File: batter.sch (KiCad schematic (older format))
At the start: 6 parts, among them U2 MCP73831-SOT-23-5, U3 NCP4681-SC-70

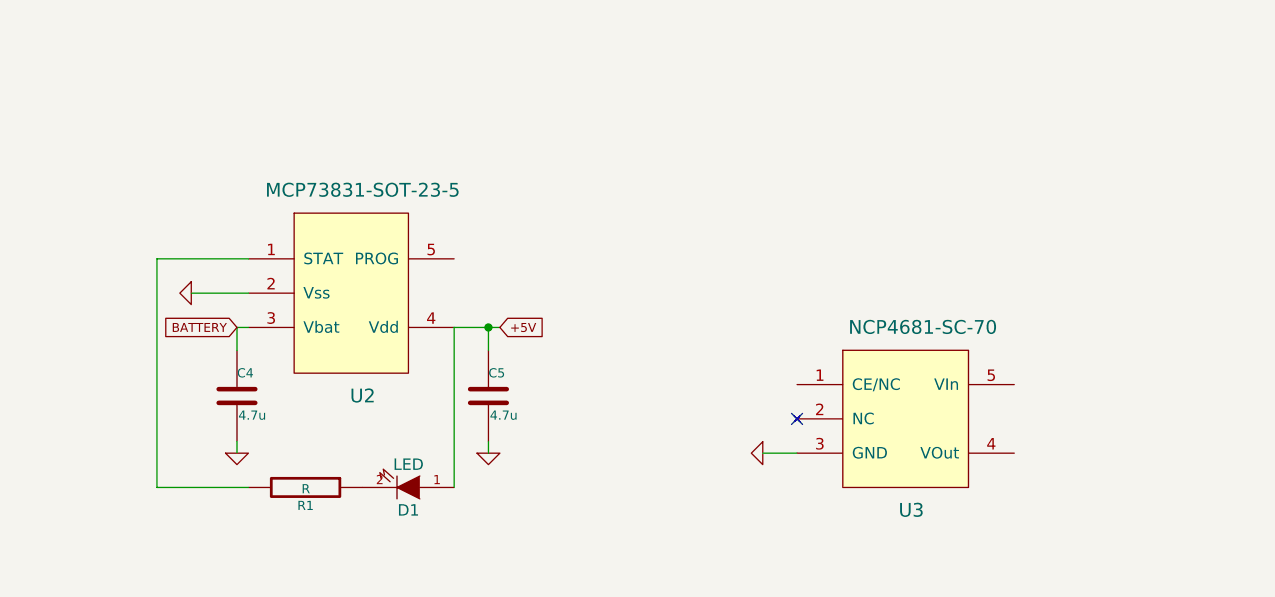
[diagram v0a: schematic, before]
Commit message: Add gps
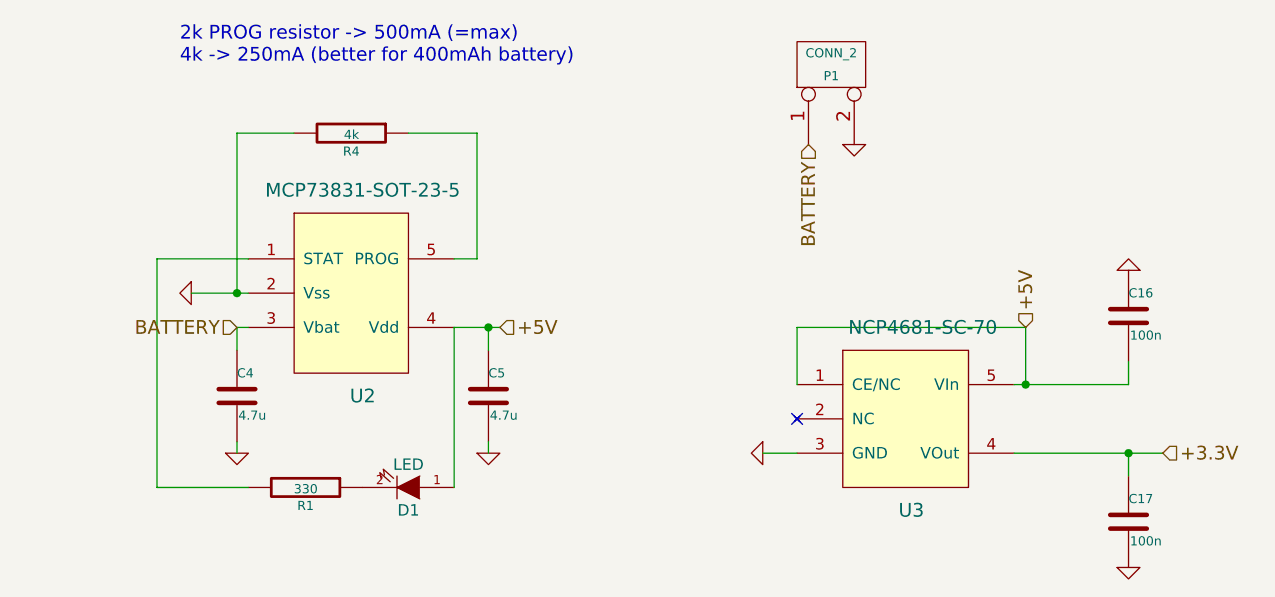
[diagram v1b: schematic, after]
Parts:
- added C16, C17: 100n, symbol C
- added P1: CONN_2, symbol CONN_2
- added R4: 4k, symbol R
- R1: value R -> 330
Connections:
- net +5V: now also U3.1 (CE/NC), U3.5 (VIn), C16.2
- net BATTERY: now also P1.1 (P1)
- net GND: now also C16.1, C17.2, P1.2 (PM), R4.2
- net at U2.5 (PROG): now also R4.1
- net +3.3V: now reaches U3.4 (VOut)
- net +3.3V: now also C17.1
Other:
- note added: "2k PROG resistor -> 500mA (=max)\n4k -> 250mA (better for 400mAh battery)"
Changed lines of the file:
@@
 $Descr A4 11693 8268
 encoding utf-8
-Sheet 3 10
+Sheet 3 11
 Title ""
 Date ""
@@
 $EndComp
 $Comp
-L GND #PWR3
+L GND #PWR4
 U 1 1 54461EBB
 P 3100 2200
-F 0 "#PWR3" H 3100 2200 30  0001 C CNN
+F 0 "#PWR4" H 3100 2200 30  0001 C CNN
 F 1 "GND" H 3100 2130 30  0001 C CNN
 F 2 "" H 3100 2200 60  0000 C CNN
@@
 	0    1    1    0
 $EndComp
-Text GLabel 4450 2350 2    39   Input ~ 0
-+5V
-Text GLabel 3300 2350 0    39   Input ~ 0
-BATTERY
 $Comp
 L LED D1
@@
 P 3600 3050
 F 0 "R1" V 3680 3050 40  0000 C CNN
-F 1 "R" V 3607 3051 40  0000 C CNN
+F 1 "330" V 3607 3051 40  0000 C CNN
 F 2 "" V 3530 3050 30  0001 C CNN
 F 3 "" H 3600 3050 30  0000 C CNN
@@
 $EndComp
 $Comp
-L GND #PWR5
+L GND #PWR6
 U 1 1 54461ED8
 P 4400 2900
-F 0 "#PWR5" H 4400 2900 30  0001 C CNN
+F 0 "#PWR6" H 4400 2900 30  0001 C CNN
 F 1 "GND" H 4400 2830 30  0001 C CNN
 F 2 "" H 4400 2900 60  0000 C CNN
@@
 $EndComp
 $Comp
-L GND #PWR4
+L GND #PWR5
 U 1 1 54461EDE
 P 3300 2900
-F 0 "#PWR4" H 3300 2900 30  0001 C CNN
+F 0 "#PWR5" H 3300 2900 30  0001 C CNN
 F 1 "GND" H 3300 2830 30  0001 C CNN
 F 2 "" H 3300 2900 60  0000 C CNN
@@
 NoConn ~ 5750 2750
 $Comp
-L GND #PWR6
+L GND #PWR7
 U 1 1 5446543B
 P 5600 2900
-F 0 "#PWR6" H 5600 2900 30  0001 C CNN
+F 0 "#PWR7" H 5600 2900 30  0001 C CNN
 F 1 "GND" H 5600 2830 30  0001 C CNN
 F 2 "" H 5600 2900 60  0000 C CNN
@@
 Wire Wire Line
 	5600 2900 5750 2900
+Text HLabel 3300 2350 0    60   Input ~ 0
+BATTERY
+$Comp
+L R R4
+U 1 1 546125B9
+P 3800 1500
+F 0 "R4" V 3880 1500 40  0000 C CNN
+F 1 "4k" V 3807 1501 40  0000 C CNN
+F 2 "" V 3730 1500 30  0000 C CNN
+F 3 "" H 3800 1500 30  0000 C CNN
+	1    3800 1500
+	0    1    1    0
+$EndComp
+Wire Wire Line
+	4050 1500 4350 1500
+Wire Wire Line
+	4350 1500 4350 2050
+Wire Wire Line
+	4350 2050 4250 2050
+Wire Wire Line
+	3550 1500 3300 1500
+Wire Wire Line
+	3300 1500 3300 2200
+Connection ~ 3300 2200
+Text Notes 3050 1200 0    60   ~ 0
+2k PROG resistor -> 500mA (=max)\n4k -> 250mA (better for 400mAh battery)
+Text HLabel 4450 2350 2    60   Input ~ 0
++5V
+$Comp
+L C C16
+U 1 1 54612E49
+P 7200 2300
+F 0 "C16" H 7200 2400 40  0000 L CNN
+F 1 "100n" H 7206 2215 40  0000 L CNN
+F 2 "" H 7238 2150 30  0000 C CNN
+F 3 "" H 7200 2300 60  0000 C CNN
+	1    7200 2300
+	1    0    0    -1
+$EndComp
+Wire Wire Line
+	6700 2600 7200 2600
+Wire Wire Line
+	7200 2600 7200 2500
+$Comp
+L GND #PWR9
+U 1 1 54613131
+P 7200 2100
+F 0 "#PWR9" H 7200 2100 30  0001 C CNN
+F 1 "GND" H 7200 2030 30  0001 C CNN
+F 2 "" H 7200 2100 60  0000 C CNN
+F 3 "" H 7200 2100 60  0000 C CNN
+	1    7200 2100
+	-1   0    0    1
+$EndComp
+Wire Wire Line
+	6750 2600 6750 2350
+Wire Wire Line
+	6750 2350 5750 2350
+Wire Wire Line
+	5750 2350 5750 2600
+Connection ~ 6750 2600
+$Comp
+L C C17
+U 1 1 546131AA
+P 7200 3200
+F 0 "C17" H 7200 3300 40  0000 L CNN
+F 1 "100n" H 7206 3115 40  0000 L CNN
+F 2 "" H 7238 3050 30  0000 C CNN
+F 3 "" H 7200 3200 60  0000 C CNN
+	1    7200 3200
+	1    0    0    -1
+$EndComp
+Wire Wire Line
+	6700 2900 7350 2900
+Wire Wire Line
+	7200 2900 7200 3000
+$Comp
+L GND #PWR10
+U 1 1 5461320E
+P 7200 3400
+F 0 "#PWR10" H 7200 3400 30  0001 C CNN
+F 1 "GND" H 7200 3330 30  0001 C CNN
+F 2 "" H 7200 3400 60  0000 C CNN
+F 3 "" H 7200 3400 60  0000 C CNN
+	1    7200 3400
+	1    0    0    -1
+$EndComp
+Connection ~ 7200 2900
+Text HLabel 6750 2350 1    60   Input ~ 0
++5V
+Text HLabel 7350 2900 2    60   Input ~ 0
++3.3V
+$Comp
+L CONN_2 P1
+U 1 1 5461388F
+P 5900 1200
+F 0 "P1" V 5850 1200 40  0000 C CNN
+F 1 "CONN_2" V 5950 1200 40  0000 C CNN
+F 2 "" H 5900 1200 60  0000 C CNN
+F 3 "" H 5900 1200 60  0000 C CNN
+	1    5900 1200
+	0    -1   -1   0
+$EndComp
+Text HLabel 5800 1550 3    60   Input ~ 0
+BATTERY
+$Comp
+L GND #PWR8
+U 1 1 546139D5
+P 6000 1550
+F 0 "#PWR8" H 6000 1550 30  0001 C CNN
+F 1 "GND" H 6000 1480 30  0001 C CNN
+F 2 "" H 6000 1550 60  0000 C CNN
+F 3 "" H 6000 1550 60  0000 C CNN
+	1    6000 1550
+	1    0    0    -1
+$EndComp
 $EndSCHEMATC

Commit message: More connections
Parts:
- C16, C17, D1, R1, R4: footprint (none) -> buq2:SM0603
- C4, C5: footprint (none) -> buq2:SM0805
- P1: footprint (none) -> buq2:PIN_HEADER_2
- U2: footprint (none) -> buq2:SOT-23-5
- U3: footprint (none) -> buq2:SOT-353
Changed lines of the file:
@@
 F 0 "U2" H 3850 2650 60  0000 C CNN
 F 1 "MCP73831-SOT-23-5" H 3850 3550 60  0000 C CNN
-F 2 "" H 3850 2650 60  0001 C CNN
+F 2 "buq2:SOT-23-5" H 3850 2650 60  0001 C CNN
 F 3 "" H 3850 2650 60  0000 C CNN
 	1    3850 2650
@@
 $EndComp
 $Comp
-L GND #PWR4
+L GND #PWR04
 U 1 1 54461EBB
 P 3100 2200
-F 0 "#PWR4" H 3100 2200 30  0001 C CNN
+F 0 "#PWR04" H 3100 2200 30  0001 C CNN
 F 1 "GND" H 3100 2130 30  0001 C CNN
 F 2 "" H 3100 2200 60  0000 C CNN
@@
 F 0 "D1" H 4050 3150 50  0000 C CNN
 F 1 "LED" H 4050 2950 50  0000 C CNN
-F 2 "" H 4050 3050 60  0001 C CNN
+F 2 "buq2:SM0603" H 4050 3050 60  0001 C CNN
 F 3 "" H 4050 3050 60  0000 C CNN
 	1    4050 3050
@@
 F 0 "R1" V 3680 3050 40  0000 C CNN
 F 1 "330" V 3607 3051 40  0000 C CNN
-F 2 "" V 3530 3050 30  0001 C CNN
+F 2 "buq2:SM0603" V 3530 3050 30  0001 C CNN
 F 3 "" H 3600 3050 30  0000 C CNN
 	1    3600 3050
@@
 F 0 "C5" H 4400 2750 40  0000 L CNN
 F 1 "4.7u" H 4406 2565 40  0000 L CNN
-F 2 "" H 4438 2500 30  0001 C CNN
+F 2 "buq2:SM0805" H 4438 2500 30  0001 C CNN
 F 3 "" H 4400 2650 60  0000 C CNN
 	1    4400 2650
@@
 $EndComp
 $Comp
-L GND #PWR6
+L GND #PWR05
 U 1 1 54461ED8
 P 4400 2900
-F 0 "#PWR6" H 4400 2900 30  0001 C CNN
+F 0 "#PWR05" H 4400 2900 30  0001 C CNN
 F 1 "GND" H 4400 2830 30  0001 C CNN
 F 2 "" H 4400 2900 60  0000 C CNN
@@
 $EndComp
 $Comp
-L GND #PWR5
+L GND #PWR06
 U 1 1 54461EDE
 P 3300 2900
-F 0 "#PWR5" H 3300 2900 30  0001 C CNN
+F 0 "#PWR06" H 3300 2900 30  0001 C CNN
 F 1 "GND" H 3300 2830 30  0001 C CNN
 F 2 "" H 3300 2900 60  0000 C CNN
@@
 F 0 "C4" H 3300 2750 40  0000 L CNN
 F 1 "4.7u" H 3306 2565 40  0000 L CNN
-F 2 "" H 3338 2500 30  0001 C CNN
+F 2 "buq2:SM0805" H 3338 2500 30  0001 C CNN
 F 3 "" H 3300 2650 60  0000 C CNN
 	1    3300 2650
@@
 F 0 "U3" H 6250 2250 60  0000 C CNN
 F 1 "NCP4681-SC-70" H 6300 3050 60  0000 C CNN
-F 2 "" H 6250 2150 60  0001 C CNN
+F 2 "buq2:SOT-353" H 6250 2150 60  0001 C CNN
 F 3 "" H 6250 2150 60  0000 C CNN
 	1    6250 2700
@@
 NoConn ~ 5750 2750
 $Comp
-L GND #PWR7
+L GND #PWR07
 U 1 1 5446543B
 P 5600 2900
-F 0 "#PWR7" H 5600 2900 30  0001 C CNN
+F 0 "#PWR07" H 5600 2900 30  0001 C CNN
 F 1 "GND" H 5600 2830 30  0001 C CNN
 F 2 "" H 5600 2900 60  0000 C CNN
@@
 F 0 "R4" V 3880 1500 40  0000 C CNN
 F 1 "4k" V 3807 1501 40  0000 C CNN
-F 2 "" V 3730 1500 30  0000 C CNN
+F 2 "buq2:SM0603" V 3730 1500 30  0001 C CNN
 F 3 "" H 3800 1500 30  0000 C CNN
 	1    3800 1500
@@
 F 0 "C16" H 7200 2400 40  0000 L CNN
 F 1 "100n" H 7206 2215 40  0000 L CNN
-F 2 "" H 7238 2150 30  0000 C CNN
+F 2 "buq2:SM0603" H 7238 2150 30  0001 C CNN
 F 3 "" H 7200 2300 60  0000 C CNN
 	1    7200 2300
@@
 	7200 2600 7200 2500
 $Comp
-L GND #PWR9
+L GND #PWR08
 U 1 1 54613131
 P 7200 2100
-F 0 "#PWR9" H 7200 2100 30  0001 C CNN
+F 0 "#PWR08" H 7200 2100 30  0001 C CNN
 F 1 "GND" H 7200 2030 30  0001 C CNN
 F 2 "" H 7200 2100 60  0000 C CNN
@@
 F 0 "C17" H 7200 3300 40  0000 L CNN
 F 1 "100n" H 7206 3115 40  0000 L CNN
-F 2 "" H 7238 3050 30  0000 C CNN
+F 2 "buq2:SM0603" H 7238 3050 30  0001 C CNN
 F 3 "" H 7200 3200 60  0000 C CNN
 	1    7200 3200
@@
 	7200 2900 7200 3000
 $Comp
-L GND #PWR10
+L GND #PWR09
 U 1 1 5461320E
 P 7200 3400
-F 0 "#PWR10" H 7200 3400 30  0001 C CNN
+F 0 "#PWR09" H 7200 3400 30  0001 C CNN
 F 1 "GND" H 7200 3330 30  0001 C CNN
 F 2 "" H 7200 3400 60  0000 C CNN
@@
 F 0 "P1" V 5850 1200 40  0000 C CNN
 F 1 "CONN_2" V 5950 1200 40  0000 C CNN
-F 2 "" H 5900 1200 60  0000 C CNN
+F 2 "buq2:PIN_HEADER_2" H 5900 1200 60  0001 C CNN
 F 3 "" H 5900 1200 60  0000 C CNN
 	1    5900 1200
@@
 BATTERY
 $Comp
-L GND #PWR8
+L GND #PWR010
 U 1 1 546139D5
 P 6000 1550
-F 0 "#PWR8" H 6000 1550 30  0001 C CNN
+F 0 "#PWR010" H 6000 1550 30  0001 C CNN
 F 1 "GND" H 6000 1480 30  0001 C CNN
 F 2 "" H 6000 1550 60  0000 C CNN

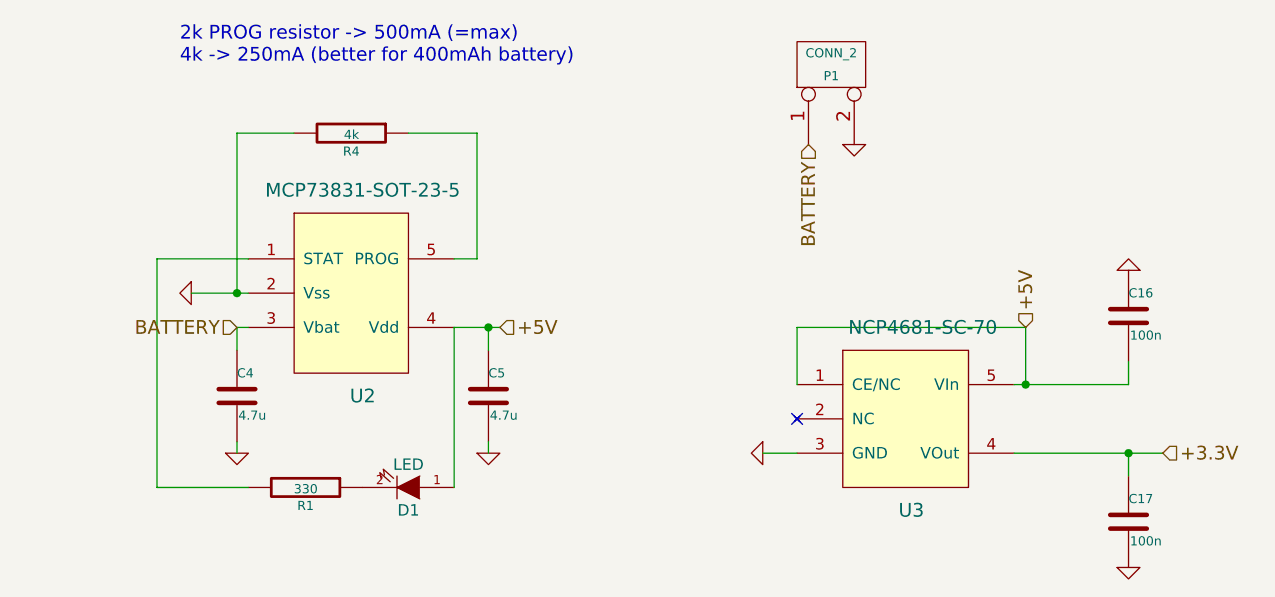
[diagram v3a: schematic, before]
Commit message: Add flash and ram. Some connections and DRC cleaning
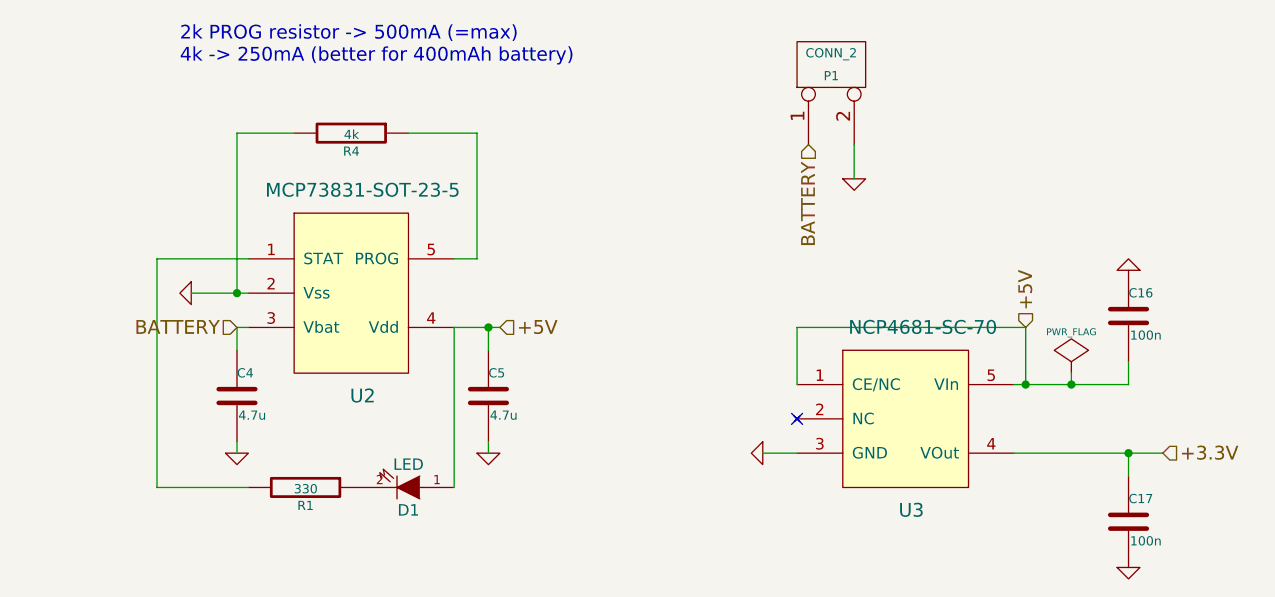
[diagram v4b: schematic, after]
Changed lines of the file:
@@
 $Descr A4 11693 8268
 encoding utf-8
-Sheet 3 12
+Sheet 3 13
 Title ""
 Date ""
@@
 L GND #PWR010
 U 1 1 546139D5
-P 6000 1550
-F 0 "#PWR010" H 6000 1550 30  0001 C CNN
-F 1 "GND" H 6000 1480 30  0001 C CNN
-F 2 "" H 6000 1550 60  0000 C CNN
-F 3 "" H 6000 1550 60  0000 C CNN
-	1    6000 1550
-	1    0    0    -1
-$EndComp
+P 6000 1700
+F 0 "#PWR010" H 6000 1700 30  0001 C CNN
+F 1 "GND" H 6000 1630 30  0001 C CNN
+F 2 "" H 6000 1700 60  0000 C CNN
+F 3 "" H 6000 1700 60  0000 C CNN
+	1    6000 1700
+	1    0    0    -1
+$EndComp
+$Comp
+L PWR_FLAG #FLG011
+U 1 1 54649A02
+P 6950 2550
+F 0 "#FLG011" H 6950 2645 30  0001 C CNN
+F 1 "PWR_FLAG" H 6950 2730 30  0000 C CNN
+F 2 "" H 6950 2550 60  0000 C CNN
+F 3 "" H 6950 2550 60  0000 C CNN
+	1    6950 2550
+	1    0    0    -1
+$EndComp
+Wire Wire Line
+	6950 2550 6950 2600
+Connection ~ 6950 2600
+Wire Wire Line
+	6000 1550 6000 1700
 $EndSCHEMATC

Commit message: Add buttons. Fix DRC. Add antenna
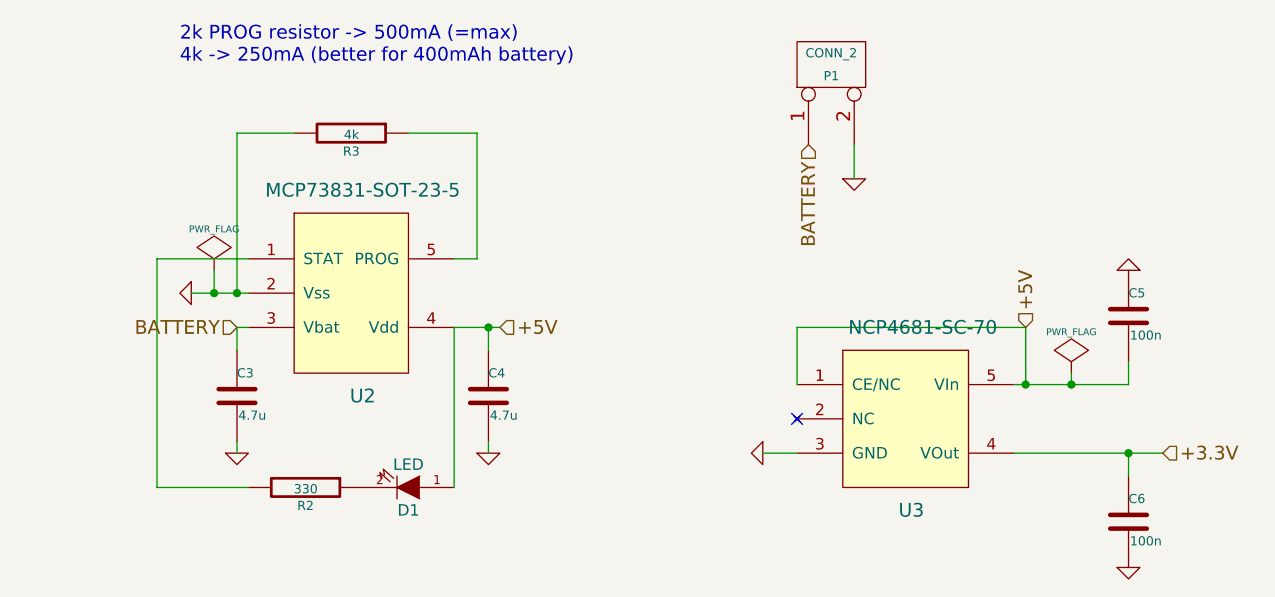
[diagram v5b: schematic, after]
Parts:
- renumbered C4 to C3, C5 to C4, C16 to C5, C17 to C6, R1 to R2, R4 to R3
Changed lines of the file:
@@
 $Descr A4 11693 8268
 encoding utf-8
-Sheet 3 13
+Sheet 3 14
 Title ""
 Date ""
@@
 $EndComp
 $Comp
-L R R1
+L R R2
 U 1 1 54461ECA
 P 3600 3050
-F 0 "R1" V 3680 3050 40  0000 C CNN
+F 0 "R2" V 3680 3050 40  0000 C CNN
 F 1 "330" V 3607 3051 40  0000 C CNN
 F 2 "buq2:SM0603" V 3530 3050 30  0001 C CNN
@@
 $EndComp
 $Comp
-L C C5
+L C C4
 U 1 1 54461ED1
 P 4400 2650
-F 0 "C5" H 4400 2750 40  0000 L CNN
+F 0 "C4" H 4400 2750 40  0000 L CNN
 F 1 "4.7u" H 4406 2565 40  0000 L CNN
 F 2 "buq2:SM0805" H 4438 2500 30  0001 C CNN
@@
 $EndComp
 $Comp
-L C C4
+L C C3
 U 1 1 54461EE4
 P 3300 2650
-F 0 "C4" H 3300 2750 40  0000 L CNN
+F 0 "C3" H 3300 2750 40  0000 L CNN
 F 1 "4.7u" H 3306 2565 40  0000 L CNN
 F 2 "buq2:SM0805" H 3338 2500 30  0001 C CNN
@@
 BATTERY
 $Comp
-L R R4
+L R R3
 U 1 1 546125B9
 P 3800 1500
-F 0 "R4" V 3880 1500 40  0000 C CNN
+F 0 "R3" V 3880 1500 40  0000 C CNN
 F 1 "4k" V 3807 1501 40  0000 C CNN
 F 2 "buq2:SM0603" V 3730 1500 30  0001 C CNN
@@
 +5V
 $Comp
-L C C16
+L C C5
 U 1 1 54612E49
 P 7200 2300
-F 0 "C16" H 7200 2400 40  0000 L CNN
+F 0 "C5" H 7200 2400 40  0000 L CNN
 F 1 "100n" H 7206 2215 40  0000 L CNN
 F 2 "buq2:SM0603" H 7238 2150 30  0001 C CNN
@@
 Connection ~ 6750 2600
 $Comp
-L C C17
+L C C6
 U 1 1 546131AA
 P 7200 3200
-F 0 "C17" H 7200 3300 40  0000 L CNN
+F 0 "C6" H 7200 3300 40  0000 L CNN
 F 1 "100n" H 7206 3115 40  0000 L CNN
 F 2 "buq2:SM0603" H 7238 3050 30  0001 C CNN
@@
 Wire Wire Line
 	6000 1550 6000 1700
+$Comp
+L PWR_FLAG #FLG012
+U 1 1 5463E2BC
+P 3200 2100
+F 0 "#FLG012" H 3200 2195 30  0001 C CNN
+F 1 "PWR_FLAG" H 3200 2280 30  0000 C CNN
+F 2 "" H 3200 2100 60  0000 C CNN
+F 3 "" H 3200 2100 60  0000 C CNN
+	1    3200 2100
+	1    0    0    -1
+$EndComp
+Wire Wire Line
+	3200 2100 3200 2200
+Connection ~ 3200 2200
 $EndSCHEMATC

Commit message: Start planning test board v2.0
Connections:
- net +5V: no longer C5.2, U3.1 (CE/NC), U3.5 (VIn)
- net BATTERY: now also C5.2, U3.1 (CE/NC), U3.5 (VIn)
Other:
- moved on the sheet: P1
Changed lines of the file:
@@
 $Descr A4 11693 8268
 encoding utf-8
-Sheet 3 14
+Sheet 3 10
 Title ""
 Date ""
@@
 $EndComp
 Connection ~ 7200 2900
-Text HLabel 6750 2350 1    60   Input ~ 0
-+5V
 Text HLabel 7350 2900 2    60   Input ~ 0
 +3.3V
@@
 L CONN_2 P1
 U 1 1 5461388F
-P 5900 1200
-F 0 "P1" V 5850 1200 40  0000 C CNN
-F 1 "CONN_2" V 5950 1200 40  0000 C CNN
-F 2 "buq2:PIN_HEADER_2" H 5900 1200 60  0001 C CNN
-F 3 "" H 5900 1200 60  0000 C CNN
-	1    5900 1200
+P 2550 1350
+F 0 "P1" V 2500 1350 40  0000 C CNN
+F 1 "CONN_2" V 2600 1350 40  0000 C CNN
+F 2 "buq2:PIN_HEADER_2" H 2550 1350 60  0001 C CNN
+F 3 "" H 2550 1350 60  0000 C CNN
+	1    2550 1350
 	0    -1   -1   0
 $EndComp
-Text HLabel 5800 1550 3    60   Input ~ 0
+Text HLabel 2450 1700 3    60   Input ~ 0
 BATTERY
 $Comp
 L GND #PWR010
 U 1 1 546139D5
-P 6000 1700
-F 0 "#PWR010" H 6000 1700 30  0001 C CNN
-F 1 "GND" H 6000 1630 30  0001 C CNN
-F 2 "" H 6000 1700 60  0000 C CNN
-F 3 "" H 6000 1700 60  0000 C CNN
-	1    6000 1700
+P 2650 1850
+F 0 "#PWR010" H 2650 1850 30  0001 C CNN
+F 1 "GND" H 2650 1780 30  0001 C CNN
+F 2 "" H 2650 1850 60  0000 C CNN
+F 3 "" H 2650 1850 60  0000 C CNN
+	1    2650 1850
 	1    0    0    -1
 $EndComp
@@
 Connection ~ 6950 2600
 Wire Wire Line
-	6000 1550 6000 1700
+	2650 1700 2650 1850
 $Comp
 L PWR_FLAG #FLG012
@@
 	3200 2100 3200 2200
 Connection ~ 3200 2200
+Text HLabel 6750 2350 1    60   Input ~ 0
+BATTERY
 $EndSCHEMATC
